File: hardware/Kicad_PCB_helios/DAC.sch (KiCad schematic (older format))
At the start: 4 parts, among them U5 DAC084S085C

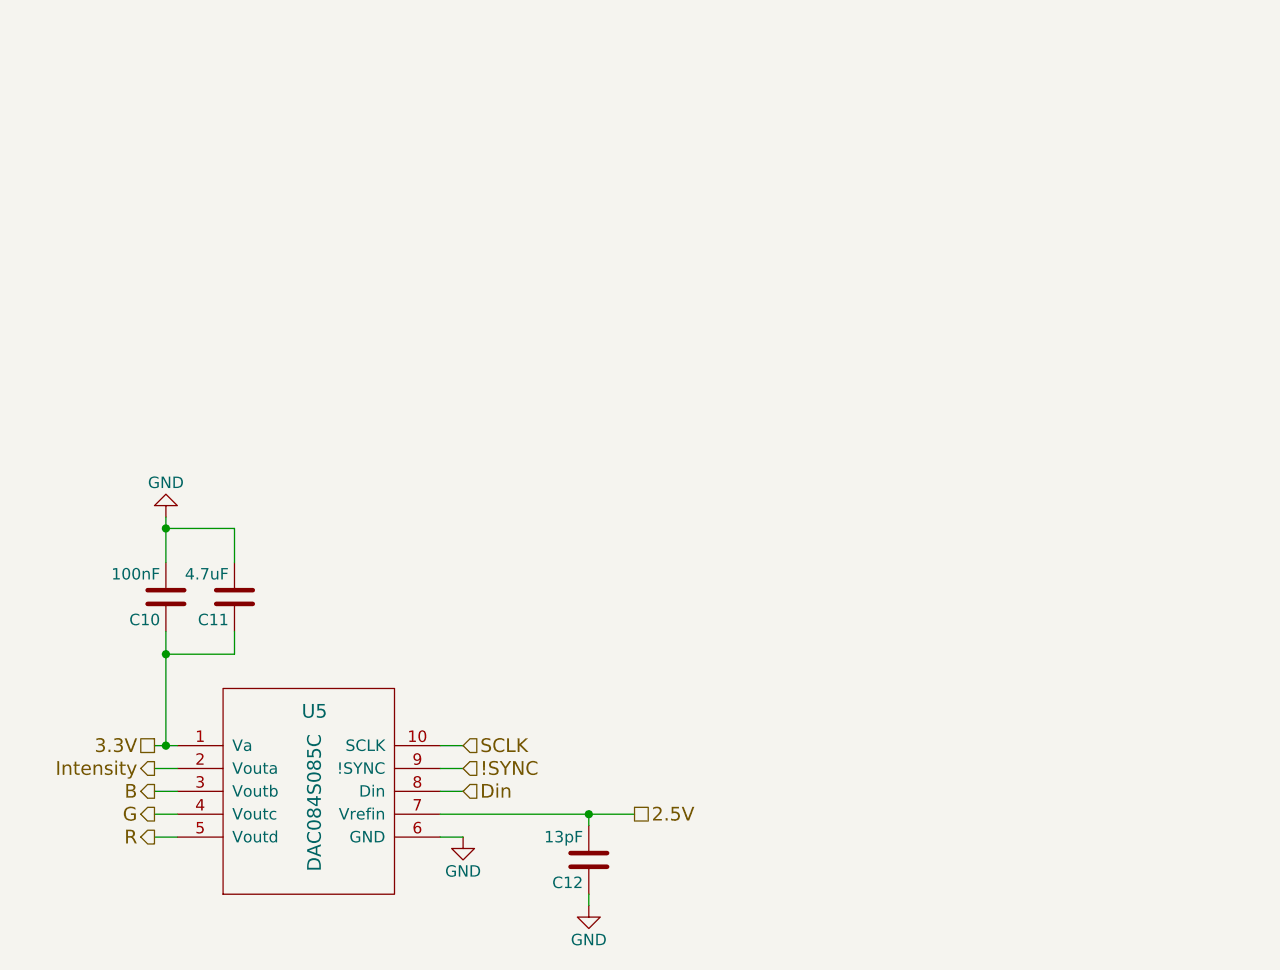
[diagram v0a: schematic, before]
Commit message: Dodano 2 zewnętrzne 16 bitowe układy DAC
Podłączono VREF do wewnętrznych DAC

Wszystko działa na jednej magistrali SPI
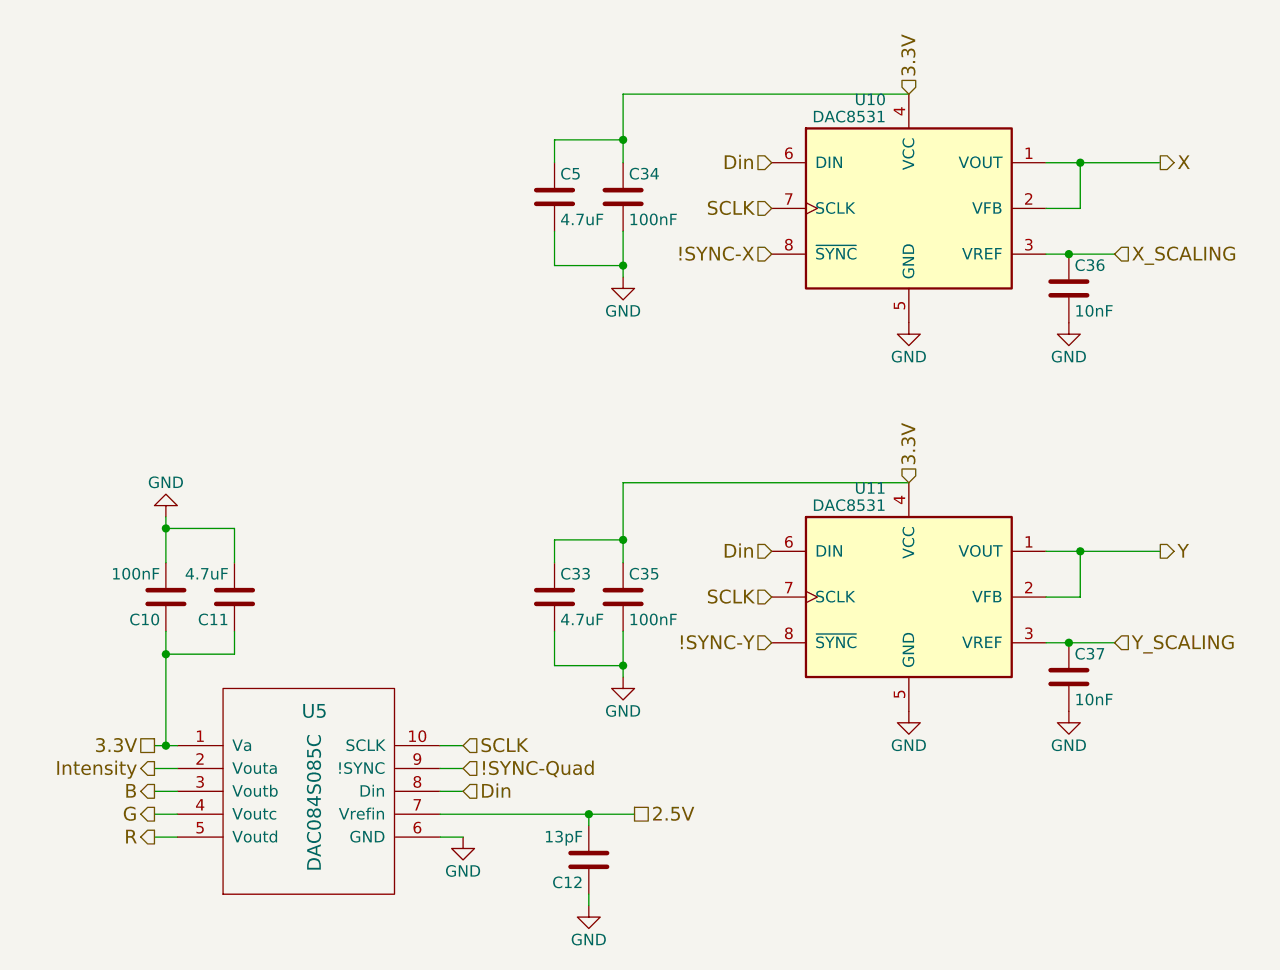
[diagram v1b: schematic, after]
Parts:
- added C33, C5: 4.7uF, Capacitors_SMD:c_elec_4x5.3, symbol C
- added C34, C35: 100nF, Capacitors_SMD:C_0402, symbol C
- added C36, C37: 10nF, Capacitors_SMD:C_0402, symbol C
- added U10, U11: DAC8531, TO_SOT_Packages_SMD:SOT-23-8_Handsoldering, symbol DAC8531
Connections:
- net 3.3V: now also C33.1, C34.1, C35.1, C5.1, U10.4 (VCC), U11.4 (VCC)
- net Din: now also U10.6 (DIN), U11.6 (DIN)
- net GND: now also C33.2, C34.2, C35.2, C36.2, C37.2, C5.2, U10.5 (GND), U11.5 (GND)
- net SCLK: now also U10.7 (SCLK), U11.7 (SCLK)
- net !SYNC renamed !SYNC-Quad
- new net !SYNC-X: U10.8 (~SYNC)
- new net !SYNC-Y: U11.8 (~SYNC)
- new net X: U10.1 (VOUT), U10.2 (VFB)
- new net X_SCALING: C36.1, U10.3 (VREF)
- new net Y: U11.1 (VOUT), U11.2 (VFB)
- new net Y_SCALING: C37.1, U11.3 (VREF)

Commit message: Updated PCB Layout
Changed connector to IDC
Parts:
- C10, C12, C34, C35, C36, C37: footprint Capacitors_SMD:C_0402 -> Capacitors_SMD:C_0603
- C33: footprint Capacitors_SMD:c_elec_4x5.3 -> (none)
- C5: footprint Capacitors_SMD:c_elec_4x5.3 -> Capacitors_SMD:CP_Elec_4x5.3
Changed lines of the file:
@@
 F 0 "C10" H 4625 3700 50  0000 L CNN
 F 1 "100nF" H 4625 3500 50  0000 L CNN
-F 2 "Capacitors_SMD:C_0402" H 4638 3450 50  0001 C CNN
+F 2 "Capacitors_SMD:C_0603" H 4638 3450 50  0001 C CNN
 F 3 "" H 4600 3600 50  0000 C CNN
 	1    4600 3600
@@
 2.5V
 $Comp
-L GND #PWR015
+L GND #PWR020
 U 1 1 56B430BD
 P 4600 3250
-F 0 "#PWR015" H 4600 3000 50  0001 C CNN
+F 0 "#PWR020" H 4600 3000 50  0001 C CNN
 F 1 "GND" H 4600 3100 50  0000 C CNN
 F 2 "" H 4600 3250 50  0000 C CNN
@@
 F 0 "C12" H 6475 4850 50  0000 L CNN
 F 1 "13pF" H 6475 4650 50  0000 L CNN
-F 2 "Capacitors_SMD:C_0402" H 6488 4600 50  0001 C CNN
+F 2 "Capacitors_SMD:C_0603" H 6488 4600 50  0001 C CNN
 F 3 "" H 6450 4750 50  0000 C CNN
 	1    6450 4750
@@
 $EndComp
 $Comp
-L GND #PWR016
+L GND #PWR021
 U 1 1 57580DA3
 P 6450 4950
-F 0 "#PWR016" H 6450 4700 50  0001 C CNN
+F 0 "#PWR021" H 6450 4700 50  0001 C CNN
 F 1 "GND" H 6450 4800 50  0000 C CNN
 F 2 "" H 6450 4950 50  0000 C CNN
@@
 $EndComp
 $Comp
-L GND #PWR017
+L GND #PWR022
 U 1 1 575A7248
 P 5900 4650
-F 0 "#PWR017" H 5900 4400 50  0001 C CNN
+F 0 "#PWR022" H 5900 4400 50  0001 C CNN
 F 1 "GND" H 5900 4500 50  0000 C CNN
 F 2 "" H 5900 4650 50  0000 C CNN
@@
 3.3V
 $Comp
-L GND #PWR018
+L GND #PWR023
 U 1 1 59281D7D
 P 7850 4100
-F 0 "#PWR018" H 7850 3850 50  0001 C CNN
+F 0 "#PWR023" H 7850 3850 50  0001 C CNN
 F 1 "GND" H 7850 3950 50  0000 C CNN
 F 2 "" H 7850 4100 50  0001 C CNN
@@
 $EndComp
 $Comp
-L GND #PWR019
+L GND #PWR024
 U 1 1 59281D9D
 P 7850 2400
-F 0 "#PWR019" H 7850 2150 50  0001 C CNN
+F 0 "#PWR024" H 7850 2150 50  0001 C CNN
 F 1 "GND" H 7850 2250 50  0000 C CNN
 F 2 "" H 7850 2400 50  0001 C CNN
@@
 F 0 "C34" H 6625 1950 50  0000 L CNN
 F 1 "100nF" H 6625 1750 50  0000 L CNN
-F 2 "Capacitors_SMD:C_0402" H 6638 1700 50  0001 C CNN
+F 2 "Capacitors_SMD:C_0603" H 6638 1700 50  0001 C CNN
 F 3 "" H 6600 1850 50  0000 C CNN
 	1    6600 1850
@@
 $EndComp
 $Comp
-L GND #PWR020
+L GND #PWR025
 U 1 1 592820CE
 P 6600 2200
-F 0 "#PWR020" H 6600 1950 50  0001 C CNN
+F 0 "#PWR025" H 6600 1950 50  0001 C CNN
 F 1 "GND" H 6600 2050 50  0000 C CNN
 F 2 "" H 6600 2200 50  0000 C CNN
 F 3 "" H 6600 2200 50  0000 C CNN
 	1    6600 2200
-	1    0    0    -1
-$EndComp
-$Comp
-L C C5
-U 1 1 592820D5
-P 6300 1850
-F 0 "C5" H 6325 1950 50  0000 L CNN
-F 1 "4.7uF" H 6325 1750 50  0000 L CNN
-F 2 "Capacitors_SMD:c_elec_4x5.3" H 6338 1700 50  0001 C CNN
-F 3 "" H 6300 1850 50  0000 C CNN
-	1    6300 1850
 	1    0    0    -1
 $EndComp
@@
 F 0 "C35" H 6625 3700 50  0000 L CNN
 F 1 "100nF" H 6625 3500 50  0000 L CNN
-F 2 "Capacitors_SMD:C_0402" H 6638 3450 50  0001 C CNN
+F 2 "Capacitors_SMD:C_0603" H 6638 3450 50  0001 C CNN
 F 3 "" H 6600 3600 50  0000 C CNN
 	1    6600 3600
@@
 $EndComp
 $Comp
-L GND #PWR021
+L GND #PWR026
 U 1 1 59282410
 P 6600 3950
-F 0 "#PWR021" H 6600 3700 50  0001 C CNN
+F 0 "#PWR026" H 6600 3700 50  0001 C CNN
 F 1 "GND" H 6600 3800 50  0000 C CNN
 F 2 "" H 6600 3950 50  0000 C CNN
@@
 F 0 "C33" H 6325 3700 50  0000 L CNN
 F 1 "4.7uF" H 6325 3500 50  0000 L CNN
-F 2 "Capacitors_SMD:c_elec_4x5.3" H 6338 3450 50  0001 C CNN
+F 2 "" H 6338 3450 50  0001 C CNN
 F 3 "" H 6300 3600 50  0000 C CNN
 	1    6300 3600
@@
 F 0 "C37" H 8575 4050 50  0000 L CNN
 F 1 "10nF" H 8575 3850 50  0000 L CNN
-F 2 "Capacitors_SMD:C_0402" H 8588 3800 50  0001 C CNN
+F 2 "Capacitors_SMD:C_0603" H 8588 3800 50  0001 C CNN
 F 3 "" H 8550 3950 50  0000 C CNN
 	1    8550 3950
@@
 F 0 "C36" H 8575 2350 50  0000 L CNN
 F 1 "10nF" H 8575 2150 50  0000 L CNN
-F 2 "Capacitors_SMD:C_0402" H 8588 2100 50  0001 C CNN
+F 2 "Capacitors_SMD:C_0603" H 8588 2100 50  0001 C CNN
 F 3 "" H 8550 2250 50  0000 C CNN
 	1    8550 2250
@@
 $EndComp
 $Comp
-L GND #PWR022
+L GND #PWR027
 U 1 1 59283FE3
 P 8550 2400
-F 0 "#PWR022" H 8550 2150 50  0001 C CNN
+F 0 "#PWR027" H 8550 2150 50  0001 C CNN
 F 1 "GND" H 8550 2250 50  0000 C CNN
 F 2 "" H 8550 2400 50  0001 C CNN
@@
 $EndComp
 $Comp
-L GND #PWR023
+L GND #PWR028
 U 1 1 59284012
 P 8550 4100
-F 0 "#PWR023" H 8550 3850 50  0001 C CNN
+F 0 "#PWR028" H 8550 3850 50  0001 C CNN
 F 1 "GND" H 8550 3950 50  0000 C CNN
 F 2 "" H 8550 4100 50  0001 C CNN
@@
 Text HLabel 8750 3800 2    60   Input ~ 0
 Y_SCALING
+$Comp
+L C C5
+U 1 1 593ACBEA
+P 6300 1850
+F 0 "C5" H 6325 1950 50  0000 L CNN
+F 1 "4.7uF" H 6325 1750 50  0000 L CNN
+F 2 "Capacitors_SMD:CP_Elec_4x5.3" H 6338 1700 50  0001 C CNN
+F 3 "" H 6300 1850 50  0000 C CNN
+	1    6300 1850
+	1    0    0    -1
+$EndComp
 $EndSCHEMATC
